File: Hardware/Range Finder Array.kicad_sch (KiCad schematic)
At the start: 32 parts, among them U10 VL53L1CXV0FY1, U11 VL53L1CXV0FY1, U12 VL53L1CXV0FY1, U13 VL53L1CXV0FY1, U6 VL53L1CXV0FY1, U7 VL53L1CXV0FY1, U9 VL53L1CXV0FY1

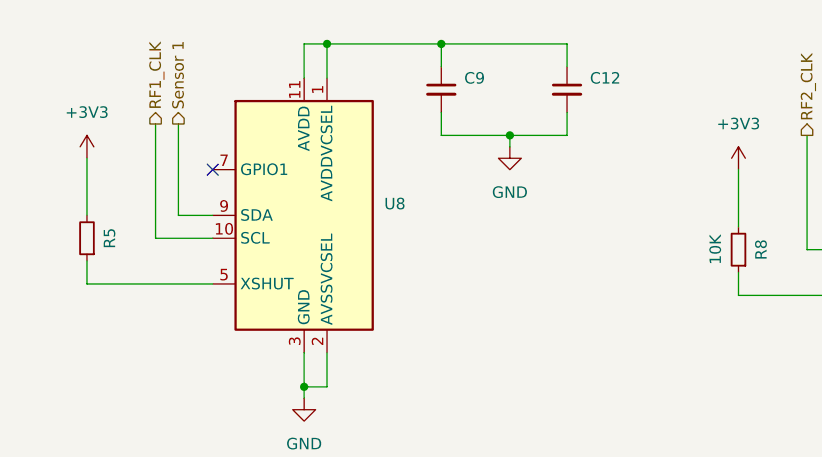
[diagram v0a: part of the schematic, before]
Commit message: Fix Reroute
Traces are getting messy, Moved the TOF sensors to be 3mm from edge of board. USB-C getting moved possibly. Changed Resistor and Capacitor footprints to better fit board space requirements.
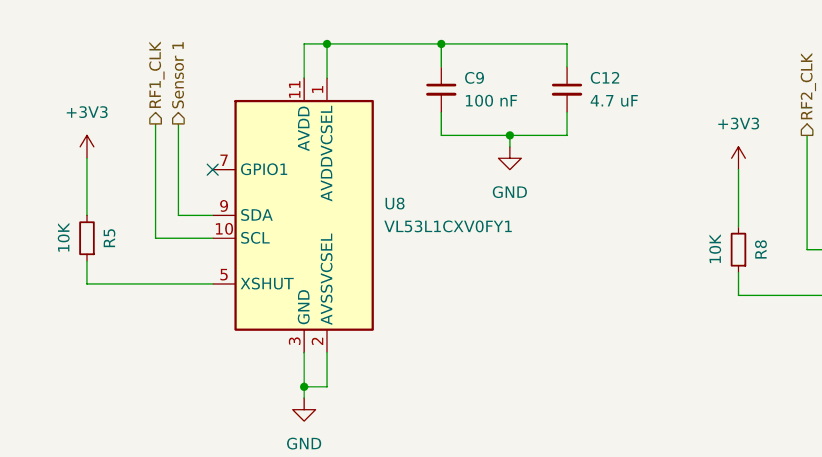
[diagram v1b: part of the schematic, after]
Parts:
- C10, C11, C13, C14, C15, C16, C17, C18, C19, C20, C21, C22, C7, C8: footprint Capacitor_SMD:C_0805_2012Metric -> Capacitor_SMD:C_0402_1005Metric
- C12: value (none) -> 4.7 uF; footprint (none) -> Capacitor_SMD:C_0402_1005Metric
- C9: value (none) -> 100 nF; footprint (none) -> Capacitor_SMD:C_0402_1005Metric
- R10, R3, R4, R6, R7, R8, R9: footprint Resistor_SMD:R_0805_2012Metric -> Resistor_SMD:R_0402_1005Metric
- R5: value (none) -> 10K; footprint (none) -> Resistor_SMD:R_0402_1005Metric
- U8: value (none) -> VL53L1CXV0FY1; footprint (none) -> Sensor_Distance:ST_VL53L1x

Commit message: Squashed commit of the following:
commit e6d18f1838a18780ff985c290e2821e2ac438ddc
Author: KenwoodFox <kenwood364@gmail.com>
Date:   Sun Oct 5 18:23:23 2025 -0400

    Tweaked n' fixed things with @Amoskeag

commit 133f082a76a13551d058af83ac953c852f82cbfb
Author: Arthur Aznive <61330561+Amoskeag@users.noreply.github.com>
Date:   Sun Oct 5 10:51:39 2025 -0400

    Update I2C Bus Connections

    Channel 4 of I2C was not connected, will make traces pretty later.

commit 1fc084a3994e8cc2965589d6eb11268a7396225d
Author: Arthur Aznive <61330561+Amoskeag@users.noreply.github.com>
Date:   Sun Oct 5 10:36:15 2025 -0400

    Board Refactor, Updated Parts

    Updated Board layout and added new parts

commit 6f7fc722645cc0153b695158322b161c2f880b4a
Author: Arthur Aznive <61330561+Amoskeag@users.noreply.github.com>
Date:   Fri Oct 3 23:22:42 2025 -0400

    update 2025

    board refactor

commit 2a13c54343b839d82b0e646e49a68070081abc7a
Author: Arthur Aznive <61330561+Amoskeag@users.noreply.github.com>
Date:   Fri Oct 3 23:04:47 2025 -0400

    Square Board Time

    Rerouting, restarting project, trying to make a simpler dev board. Lets see what we can do.

commit d4ab96b311134bb0a7992d948496d7b671a058de
Author: Arthur Aznive <61330561+Amoskeag@users.noreply.github.com>
Date:   Wed Jan 15 14:01:24 2025 -0500

    4 L:ayer Board with USB-C

    Created a 4-Layer PCB with USB-C updates

commit 55621a658c07626f43cd5cc55c172a27abc51e41
Author: Arthur Aznive <61330561+Amoskeag@users.noreply.github.com>
Date:   Tue Mar 5 00:57:37 2024 -0500

    Updated Motor Driver Routing

    Working on Power Supply and Motor Controller Routing

commit 3f2874cc29094c27990d838de84f4fea139067e1
Author: Arthur Aznive <61330561+Amoskeag@users.noreply.github.com>
Date:   Sun Mar 3 23:13:56 2024 -0500

    BIG Changes

    Create a 4 Layer Variation
    Change Motor Controller routing.
    Change Power Regulation.
    Optimize Sensor routing.
    Pray I know what i'm doing

commit 08b48da4672d4d2e9f554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
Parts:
- removed C10, C11, C12, C16, C17, C18, C21, C22: 4.7 uF, Capacitor_SMD:C_0402_1005Metric, symbol Device:C_Small
- removed C13, C14, C15, C19, C20, C7, C8, C9: 100 nF, Capacitor_SMD:C_0402_1005Metric, symbol Device:C_Small
- removed R10, R3, R4, R5, R6, R7, R8, R9: 10K, Resistor_SMD:R_0402_1005Metric, symbol Device:R_Small
- removed U10, U11, U12, U13, U6, U7, U8, U9: VL53L1CXV0FY1, Sensor_Distance:ST_VL53L1x, symbol Sensor_Distance:VL53L1CXV0FY1
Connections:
- no-connect marks 8 -> 0
